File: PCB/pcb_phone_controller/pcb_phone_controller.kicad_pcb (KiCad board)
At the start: 2 copper layers, 115.3 x 53.2 mm, 39 parts, among them SW17 SS-12D00-G 4 E, X1 KAILH-MINI-SILENT-SWITCH, Y1 KAILH-MINI-SILENT-SWITCH

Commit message: Update .gitignore and the Gerber files
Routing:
- net +3.3V: track 143.0 -> 140.3 mm
- net Net-(D3-Pad1): track 15.1 -> 12.8 mm
- net Row 0: track 145.5 -> 144.4 mm
- net Net-(TriggerR1-OUT): track 50.8 -> 49.7 mm
- net Column 1: track 137.4 -> 138.4 mm
- net Column 2: track 150.1 -> 149.4 mm
- net Net-(C1-Pad1): vias 3 -> 2
- net GND: vias 35 -> 33

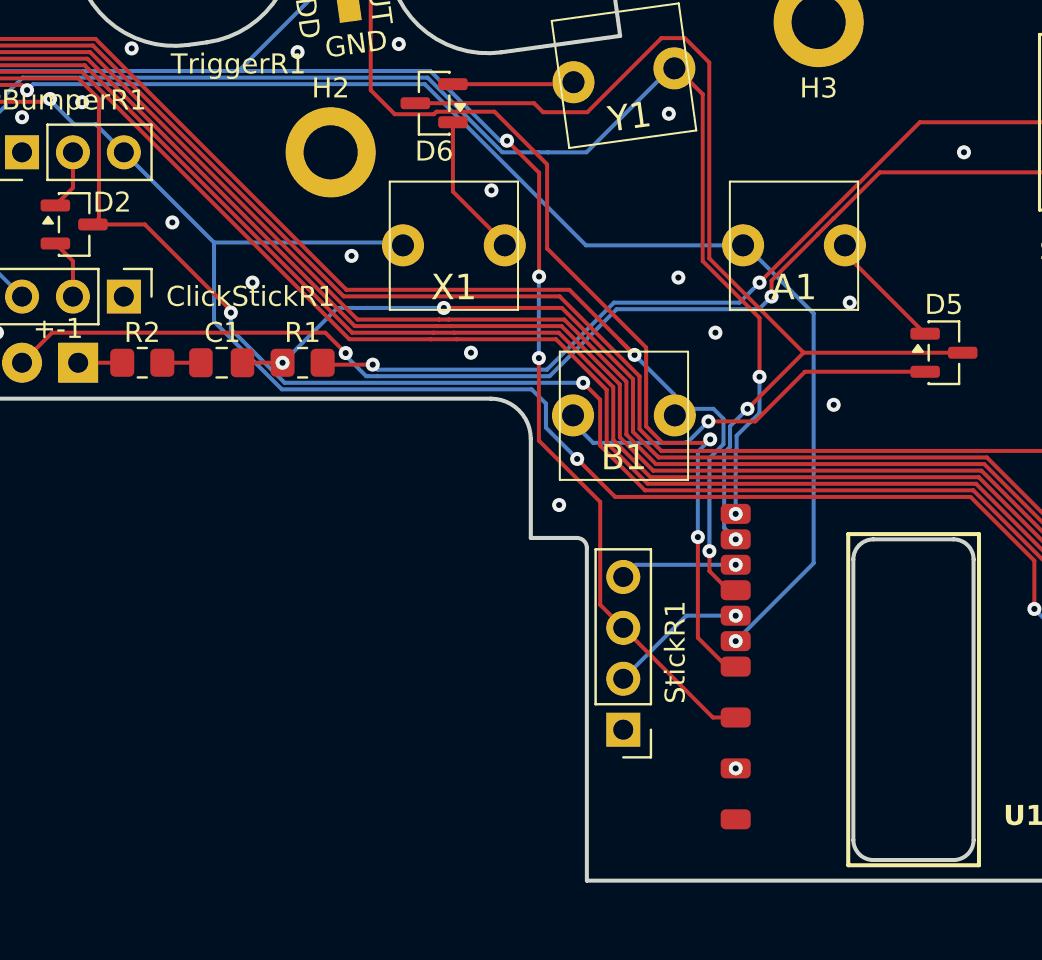
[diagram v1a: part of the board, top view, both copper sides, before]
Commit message: Add pads to connect the battery to the µcontroller + add assembly guide
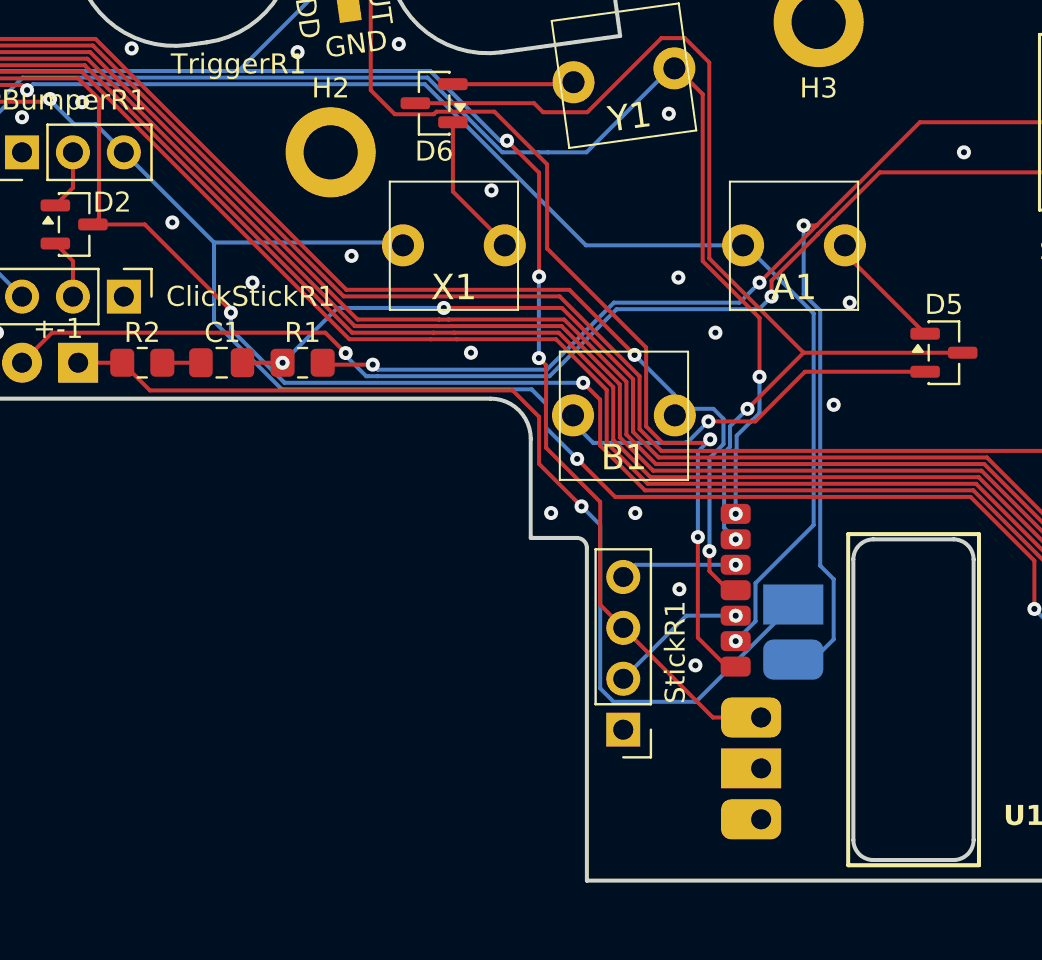
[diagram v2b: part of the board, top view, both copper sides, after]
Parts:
- A1, B1, DOWN1, Home1, LEFT1, RIGHT1, Select1, Start1, UP1, X1, Y1: value KAILH-MINI-SILENT-SWITCH -> SWITCH
- moved G*** 3.75 mm to (209.8, 125.2)
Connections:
- R1 pad 2: +BAT -> +BATT
- SW17 pad 2: +BAT -> +BATT
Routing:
- net +BATT: track 0.00 -> 67.4 mm, vias 0 -> 3
- net -BATT: track 2.25 -> 50.9 mm, vias 0 -> 1
- net +BAT: track 43.0 -> 0.00 mm, vias 2 -> 0
- net +3.3V: track 140.3 -> 141.5 mm
- net Column 1: track 138.4 -> 137.4 mm
- net GND: vias 33 -> 35

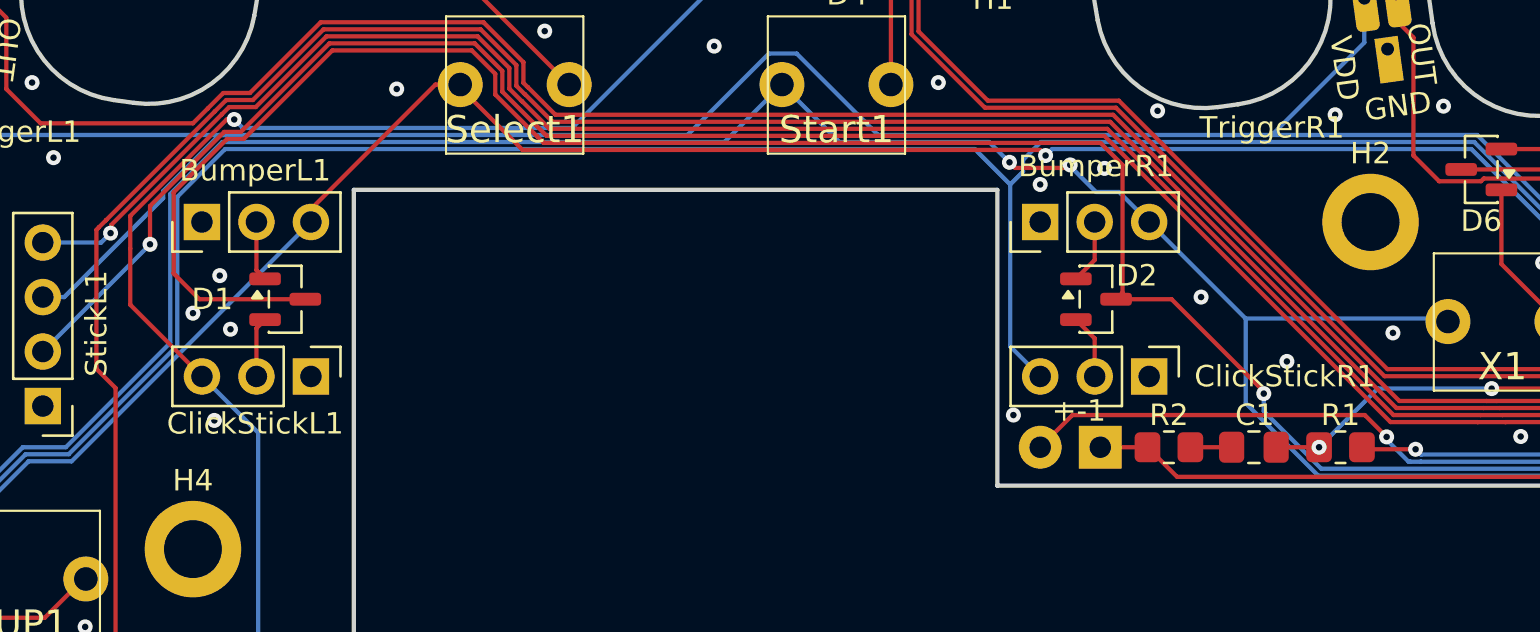
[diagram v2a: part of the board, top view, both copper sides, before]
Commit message: Add a 3D model for the TTP223
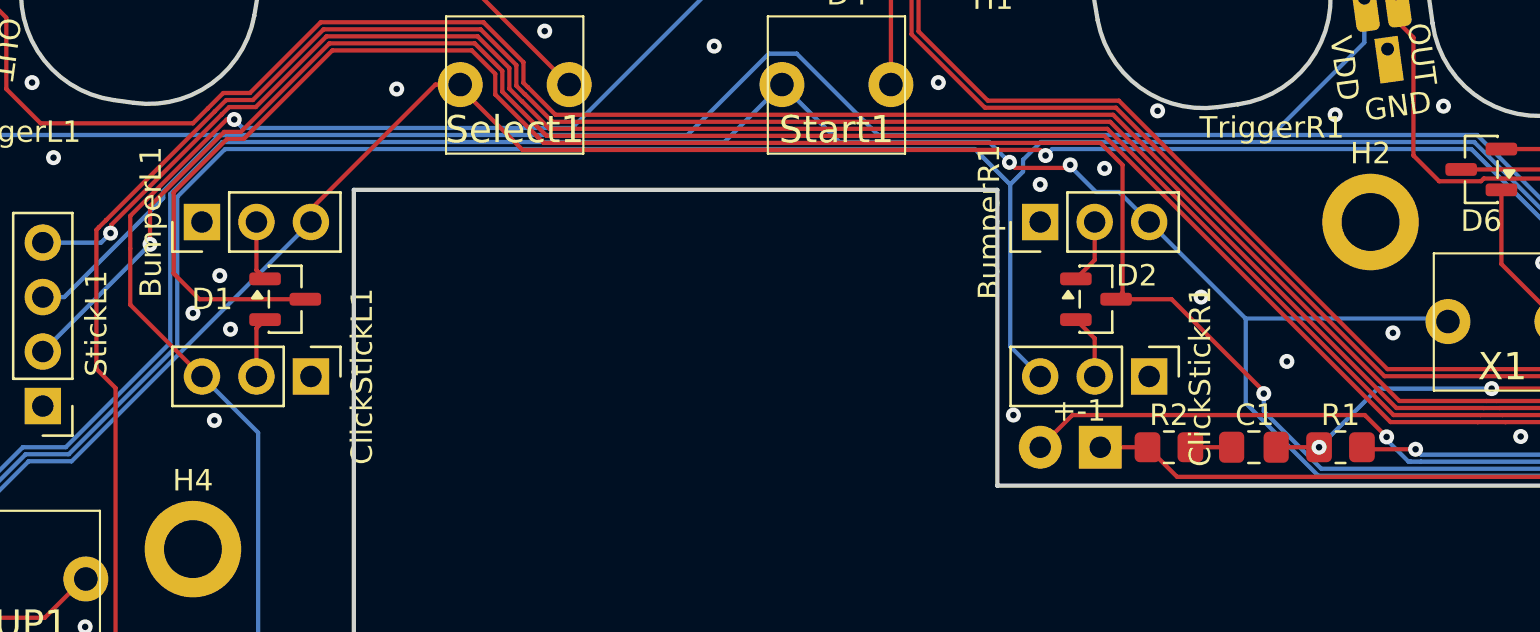
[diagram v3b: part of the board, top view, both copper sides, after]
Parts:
- A1, B1, DOWN1, Home1, LEFT1, RIGHT1, Select1, Start1, UP1, X1, Y1: value SWITCH -> KAILH-MINI-SILENT-SWITCH
- BumperL1, BumperR1, ClickStickL1, ClickStickR1: footprint Lib_controller:PinHeader_1x03_P2.54mm_Vertical -> Lib_controller:TTP223
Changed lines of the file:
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@@
 	(net 5 "Net-(C1-Pad2)")
 	(net 6 "Net-(C1-Pad1)")
-	(net 7 "Net-(+-1-BAT+)")
+	(net 7 "Net-(+-1-BATT+)")
 	(net 8 "Row 0")
 	(net 9 "Net-(BumperL1-I{slash}O)")
@@
 			)
 		)
-		(property "Value" "SWITCH"
+		(property "Value" "KAILH-MINI-SILENT-SWITCH"
 			(at 0 -2.08 0)
 			(unlocked yes)
@@
 		(embedded_fonts no)
 	)
-	(footprint "Lib_controller:PinHeader_1x03_P2.54mm_Vertical"
+	(footprint "Lib_controller:TTP223"
 		(layer "F.Cu")
 		(at 172.08 119.2 -90)
@@
 		(tags "Through hole pin header THT 1x03 2.54mm single row")
 		(property "Reference" "ClickStickR1"
-			(at 0 -6.32 180)
+			(at 0 -2.38 270)
 			(layer "F.SilkS")
 			(effects
@@
 		)
 		(property "Value" "~"
-			(at 0 7.46 90)
+			(at 0 7.46 270)
 			(layer "F.Fab")
 			(effects
@@
 		)
 		(property "Datasheet" ""
-			(at 0 0 90)
+			(at 0 0 270)
 			(layer "F.Fab")
 			(hide yes)
@@
 		)
 		(property "Description" ""
-			(at 0 0 90)
+			(at 0 0 270)
 			(layer "F.Fab")
 			(hide yes)
@@
 		)
 		(embedded_fonts no)
-		(model "${KICAD9_3DMODEL_DIR}/Connector_PinHeader_2.54mm.3dshapes/PinHeader_1x03_P2.54mm_Vertical.step"
+		(model "${KIPRJMOD}/3Dmodels/TTP223.step"
 			(offset
-				(xyz 0 0 -1.6)
+				(xyz 6 -2.54 -6.6)
 			)
 			(scale
-				(xyz 1 1 -1)
+				(xyz 1 1 1)
 			)
 			(rotate
-				(xyz -0 -0 -0)
+				(xyz -0 -0 -180)
 			)
 		)
@@
 		)
 	)
-	(footprint "Lib_controller:PinHeader_1x03_P2.54mm_Vertical"
+	(footprint "Lib_controller:TTP223"
 		(layer "F.Cu")
 		(at 133 119.2 -90)
@@
 		(tags "Through hole pin header THT 1x03 2.54mm single row")
 		(property "Reference" "ClickStickL1"
-			(at 2.2 2.6 180)
+			(at 0 -2.38 270)
 			(layer "F.SilkS")
 			(effects
@@
 		)
 		(property "Value" "~"
-			(at 0 7.46 90)
+			(at 0 7.46 270)
 			(layer "F.Fab")
 			(effects
@@
 		)
 		(property "Datasheet" ""
-			(at 0 0 90)
+			(at 0 0 270)
 			(layer "F.Fab")
 			(hide yes)
@@
 		)
 		(property "Description" ""
-			(at 0 0 90)
+			(at 0 0 270)
 			(layer "F.Fab")
 			(hide yes)
@@
 		)
 		(embedded_fonts no)
-		(model "${KICAD9_3DMODEL_DIR}/Connector_PinHeader_2.54mm.3dshapes/PinHeader_1x03_P2.54mm_Vertical.step"
+		(model "${KIPRJMOD}/3Dmodels/TTP223.step"
 			(offset
-				(xyz 0 0 -1.6)
+				(xyz 6 -2.54 -6.6)
 			)
 			(scale
-				(xyz 1 1 -1)
+				(xyz 1 1 1)
 			)
 			(rotate
-				(xyz -0 -0 -0)
+				(xyz -0 -0 -180)
 			)
 		)
@@
 			)
 		)
-		(property "Value" "SWITCH"
+		(property "Value" "KAILH-MINI-SILENT-SWITCH"
 			(at 0 -2.08 0)
 			(unlocked yes)
@@
 			(layers "*.Cu" "*.Mask")
 			(remove_unused_layers no)
-			(net 7 "Net-(+-1-BAT+)")
+			(net 7 "Net-(+-1-BATT+)")
 			(pinfunction "3")
 			(pintype "unspecified")
@@
 		(embedded_fonts no)
 	)
-	(footprint "Lib_controller:PinHeader_1x03_P2.54mm_Vertical"
+	(footprint "Lib_controller:TTP223"
 		(layer "F.Cu")
 		(at 167 112 90)
@@
 		(tags "Through hole pin header THT 1x03 2.54mm single row")
 		(property "Reference" "BumperR1"
-			(at 2.6 2.6 180)
+			(at 0 -2.38 90)
 			(layer "F.SilkS")
 			(effects
@@
 		)
 		(embedded_fonts no)
-		(model "${KICAD9_3DMODEL_DIR}/Connector_PinHeader_2.54mm.3dshapes/PinHeader_1x03_P2.54mm_Vertical.step"
+		(model "${KIPRJMOD}/3Dmodels/TTP223.step"
 			(offset
-				(xyz 0 0 -1.6)
+				(xyz 6 -2.54 -6.6)
 			)
 			(scale
-				(xyz 1 1 -1)
+				(xyz 1 1 1)
 			)
 			(rotate
-				(xyz -0 -0 -0)
+				(xyz -0 -0 -180)
 			)
 		)
@@
 			)
 		)
-		(property "Value" "SWITCH"
+		(property "Value" "KAILH-MINI-SILENT-SWITCH"
 			(at 0 -2.08 0)
 			(unlocked yes)
@@
 			)
 		)
-		(property "Value" "SWITCH"
+		(property "Value" "KAILH-MINI-SILENT-SWITCH"
 			(at 0 -2.08 0)
 			(unlocked yes)
@@
 			)
 		)
-		(property "Value" "SWITCH"
+		(property "Value" "KAILH-MINI-SILENT-SWITCH"
 			(at 0 -2.08 0)
 			(unlocked yes)
@@
 			)
 		)
-		(property "Value" "SWITCH"
+		(property "Value" "KAILH-MINI-SILENT-SWITCH"
 			(at 0 -2.08 0)
 			(unlocked yes)
@@
 			)
 		)
-		(property "Value" "SWITCH"
+		(property "Value" "KAILH-MINI-SILENT-SWITCH"
 			(at 0 -2.08 0)
 			(unlocked yes)
@@
 			)
 		)
-		(property "Value" "SWITCH"
+		(property "Value" "KAILH-MINI-SILENT-SWITCH"
 			(at 0.000002 -2.08 7.854)
 			(unlocked yes)
@@
 			(layers "*.Cu" "*.Mask")
 			(remove_unused_layers no)
-			(net 7 "Net-(+-1-BAT+)")
+			(net 7 "Net-(+-1-BATT+)")
 			(pinfunction "BATT+")
 			(pintype "power_out")
@@
 		)
 	)
-	(footprint "Lib_controller:PinHeader_1x03_P2.54mm_Vertical"
+	(footprint "Lib_controller:TTP223"
 		(layer "F.Cu")
 		(at 127.92 112 90)
@@
 		(tags "Through hole pin header THT 1x03 2.54mm single row")
 		(property "Reference" "BumperL1"
-			(at 2.4 2.48 180)
+			(at 0 -2.38 90)
 			(layer "F.SilkS")
 			(effects
@@
 		)
 		(fp_text user "${REFERENCE}"
-			(at 0 2.54 0)
+			(at 0 2.54 180)
 			(layer "F.Fab")
 			(effects
@@
 		)
 		(embedded_fonts no)
-		(model "${KICAD9_3DMODEL_DIR}/Connector_PinHeader_2.54mm.3dshapes/PinHeader_1x03_P2.54mm_Vertical.step"
+		(model "${KIPRJMOD}/3Dmodels/TTP223.step"
 			(offset
-				(xyz 0 0 -1.6)
+				(xyz 6 -2.54 -6.6)
 			)
 			(scale
-				(xyz 1 1 -1)
+				(xyz 1 1 1)
 			)
 			(rotate
-				(xyz -0 -0 -0)
+				(xyz -0 -0 -180)
 			)
 		)
@@
 			)
 		)
-		(property "Value" "SWITCH"
+		(property "Value" "KAILH-MINI-SILENT-SWITCH"
 			(at 0 -2.08 0)
 			(unlocked yes)
@@
 			)
 		)
-		(property "Value" "SWITCH"
+		(property "Value" "KAILH-MINI-SILENT-SWITCH"
 			(at 0 -2.08 0)
 			(unlocked yes)
@@
 			)
 		)
-		(property "Value" "SWITCH"
+		(property "Value" "KAILH-MINI-SILENT-SWITCH"
 			(at 0 -2.08 0)
 			(unlocked yes)
